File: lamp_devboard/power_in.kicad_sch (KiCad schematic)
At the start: 26 parts, among them J201 Screw_Terminal_01x02, J202 USB_C_Receptacle_USB2.0, U201 TLV71318PDBV, U202 TLV71318PDBV, U203 FUSB302B01MPX

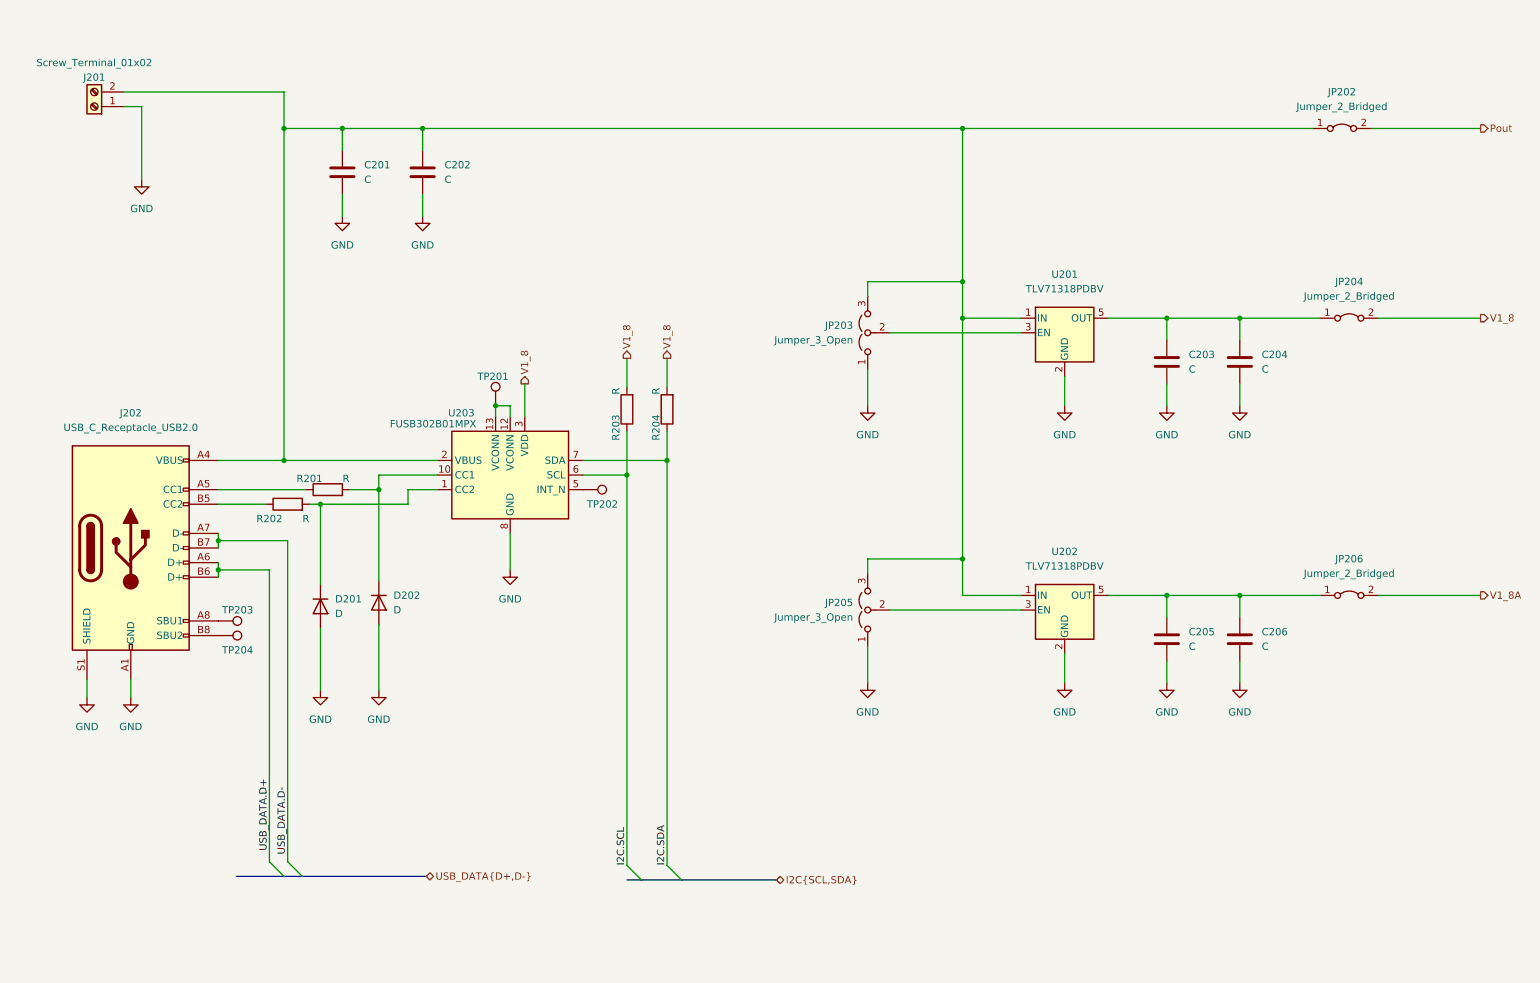
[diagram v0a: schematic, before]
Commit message: schematics, add battery to power module
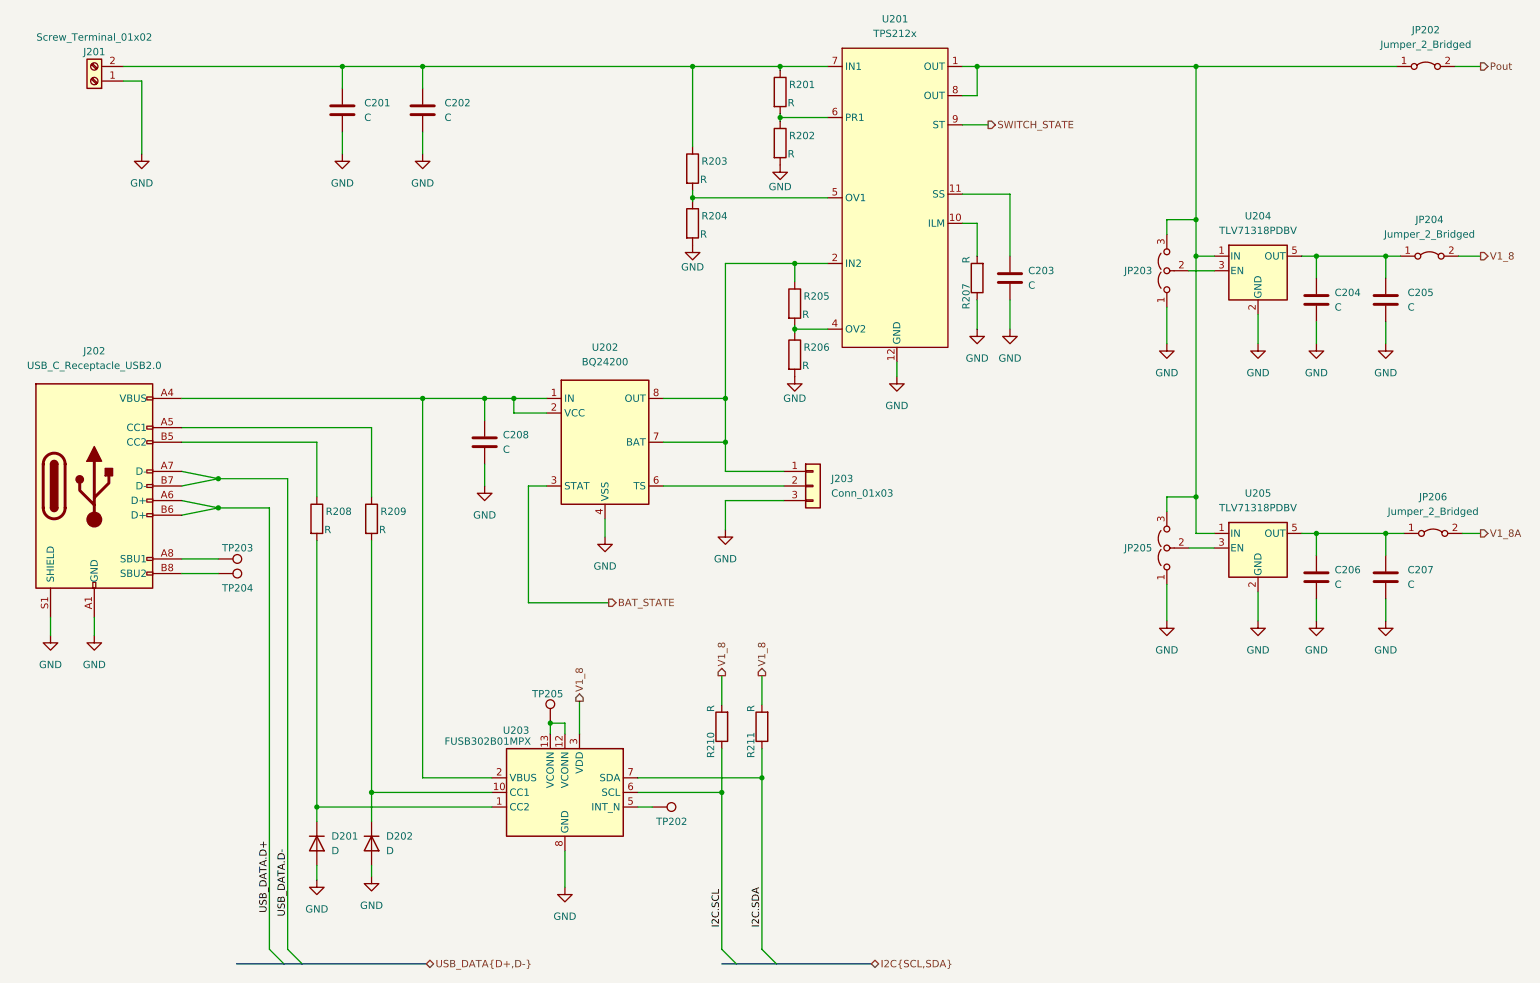
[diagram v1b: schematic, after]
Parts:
- added C203: C, Capacitor_SMD:C_0603_1608Metric_Pad1.08x0.95mm_HandSolder, symbol Device:C
- added C208: C, Capacitor_SMD:C_2220_5650Metric_Pad1.97x5.40mm_HandSolder, symbol Device:C
- added J203: Conn_01x03, Connector_Molex:Molex_KK-254_AE-6410-03A_1x03_P2.54mm_Vertical, symbol Connector_Generic:Conn_01x03
- added R201, R202, R203, R204, R205, R206, R207: R, Resistor_SMD:R_0603_1608Metric_Pad0.98x0.95mm_HandSolder, symbol Device:R
- added U201: TPS212x, lamp_devboard_lib:VQFN-HR, symbol lamp_devboard_lib:TPS212x
- added U202: BQ24200, Package_SO:HVSSOP-10-1EP_3x3mm_P0.5mm_EP1.57x1.88mm_ThermalVias, symbol lamp_devboard_lib:BQ24200
- C204: renamed from C203; footprint (none) -> Capacitor_SMD:C_0603_1608Metric_Pad1.08x0.95mm_HandSolder
- C205: renamed from C204; footprint Capacitor_SMD:C_2220_5650Metric_Pad1.97x5.40mm_HandSolder -> Capacitor_SMD:C_1206_3216Metric_Pad1.33x1.80mm_HandSolder
- C207: renamed from C206; footprint Capacitor_SMD:C_2220_5650Metric_Pad1.97x5.40mm_HandSolder -> Capacitor_SMD:C_1206_3216Metric_Pad1.33x1.80mm_HandSolder
- renumbered C205 to C206, R202 to R208, R201 to R209, R203 to R210, R204 to R211, TP201 to TP205, U201 to U204, U202 to U205
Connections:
- net GND: now also C203.2, C208.2, J203.3 (Pin_3), R202.2, R204.2, R206.2, R207.1, U201.12 (GND), U202.4 (VSS)
- new net: C201.1, C202.1, J201.2 (Pin_2), R201.1, R203.1, U201.7 (IN1)
- new net: C208.1, J202.A4 (VBUS), J202.A9 (VBUS), J202.B4 (VBUS), J202.B9 (VBUS), U202.1 (IN), U202.2 (VCC), U203.2 (VBUS)
- new net: JP202.1 (A), JP203.3 (B), JP205.3 (B), U201.1 (OUT), U201.8 (OUT), U204.1 (IN), U205.1 (IN)
- new net: R201.2, R202.1, U201.6 (PR1)
- new net: R203.2, R204.1, U201.5 (OV1)
- new net: R205.2, R206.1, U201.4 (OV2)
- new net: R207.2, U201.10 (ILM)
- new net: C203.1, U201.11 (SS)
- new net: J203.1 (Pin_1), R205.1, U201.2 (IN2), U202.7 (BAT), U202.8 (OUT)
- new net: J203.2 (Pin_2), U202.6 (TS)
- new net BAT_STATE: U202.3 (STAT)
- new net SWITCH_STATE: U201.9 (ST)
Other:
- moved on the sheet: C201, C202, C204, C205, C206, C207, D201, D202, J201, J202, JP202, JP203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

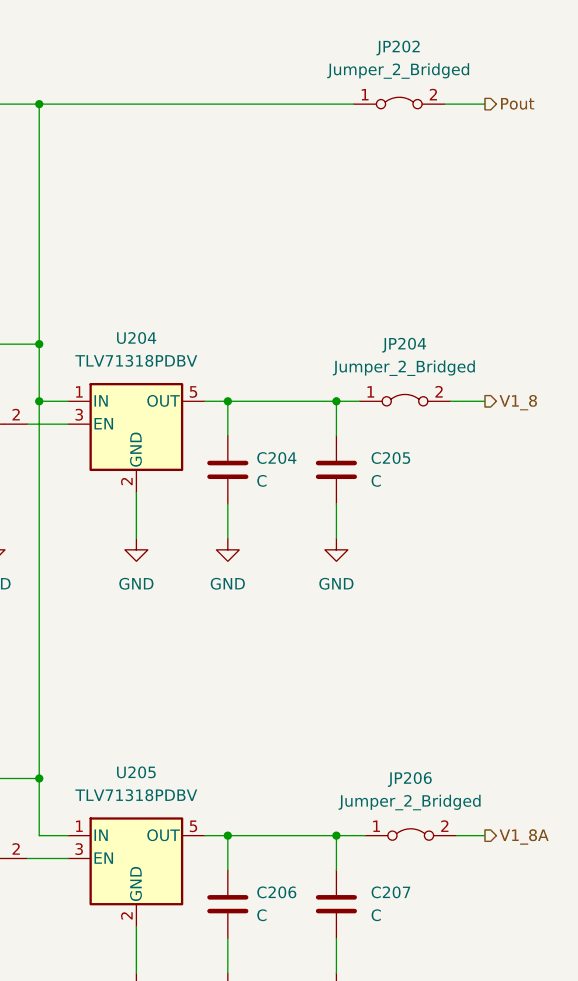
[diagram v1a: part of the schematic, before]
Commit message: place components
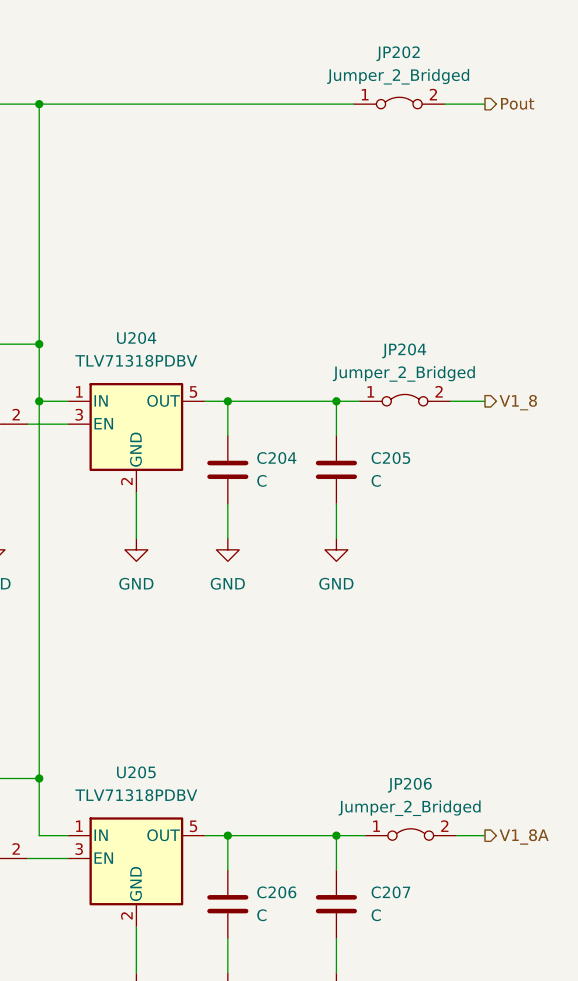
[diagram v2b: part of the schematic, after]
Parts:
- C202, C208: footprint Capacitor_SMD:C_2220_5650Metric_Pad1.97x5.40mm_HandSolder -> Capacitor_SMD:C_0603_1608Metric_Pad1.08x0.95mm_HandSolder
- JP202, JP204, JP206: footprint Connector_PinHeader_2.54mm:PinHeader_1x02_P2.54mm_Vertical -> Jumper:SolderJumper-2_P1.3mm_Bridged_RoundedPad1.0x1.5mm
- JP203, JP205: footprint Connector_PinHeader_2.54mm:PinHeader_1x03_P2.54mm_Vertical -> Jumper:SolderJumper-3_P1.3mm_Open_RoundedPad1.0x1.5mm
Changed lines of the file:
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@@
       (effects (font (size 1.27 1.27)) (justify left))
     )
-    (property "Footprint" "Capacitor_SMD:C_2220_5650Metric_Pad1.97x5.40mm_HandSolder" (id 2) (at 83.5152 38.735 0)
+    (property "Footprint" "Capacitor_SMD:C_0603_1608Metric_Pad1.08x0.95mm_HandSolder" (id 2) (at 83.5152 38.735 0)
       (effects (font (size 1.27 1.27)) hide)
     )
@@
   (symbol (lib_name "Jumper_2_Bridged_1") (lib_id "Jumper:Jumper_2_Bridged") (at 257.175 27.305 0) (unit 1)
     (in_bom yes) (on_board yes) (fields_autoplaced)
-    (property "Reference" "JP202" (id 0) (at 257.175 20.955 0))
-    (property "Value" "Jumper_2_Bridged" (id 1) (at 257.175 23.495 0))
-    (property "Footprint" "Connector_PinHeader_2.54mm:PinHeader_1x02_P2.54mm_Vertical" (id 2) (at 256.54 30.48 0)
+    (property "Reference" "JP202" (id 0) (at 257.175 21.59 0))
+    (property "Value" "Jumper_2_Bridged" (id 1) (at 257.175 24.13 0))
+    (property "Footprint" "Jumper:SolderJumper-2_P1.3mm_Bridged_RoundedPad1.0x1.5mm" (id 2) (at 256.54 30.48 0)
       (effects (font (size 1.27 1.27)) hide)
     )
@@
   (symbol (lib_name "Jumper_2_Bridged_2") (lib_id "Jumper:Jumper_2_Bridged") (at 257.81 60.325 0) (unit 1)
     (in_bom yes) (on_board yes) (fields_autoplaced)
-    (property "Reference" "JP204" (id 0) (at 257.81 53.975 0))
-    (property "Value" "Jumper_2_Bridged" (id 1) (at 257.81 56.515 0))
-    (property "Footprint" "Connector_PinHeader_2.54mm:PinHeader_1x02_P2.54mm_Vertical" (id 2) (at 257.81 63.5 0)
+    (property "Reference" "JP204" (id 0) (at 257.81 54.61 0))
+    (property "Value" "Jumper_2_Bridged" (id 1) (at 257.81 57.15 0))
+    (property "Footprint" "Jumper:SolderJumper-2_P1.3mm_Bridged_RoundedPad1.0x1.5mm" (id 2) (at 257.81 63.5 0)
       (effects (font (size 1.27 1.27)) hide)
     )
@@
       (effects (font (size 1.27 1.27)) (justify left) hide)
     )
-    (property "Footprint" "Connector_PinHeader_2.54mm:PinHeader_1x03_P2.54mm_Vertical" (id 2) (at 212.09 111.125 0)
+    (property "Footprint" "Jumper:SolderJumper-3_P1.3mm_Open_RoundedPad1.0x1.5mm" (id 2) (at 212.09 111.125 0)
       (effects (font (size 1.27 1.27)) hide)
     )
@@
   (symbol (lib_id "Jumper:Jumper_2_Bridged") (at 258.445 108.585 0) (unit 1)
     (in_bom yes) (on_board yes) (fields_autoplaced)
-    (property "Reference" "JP206" (id 0) (at 258.445 102.235 0))
-    (property "Value" "Jumper_2_Bridged" (id 1) (at 258.445 104.775 0))
-    (property "Footprint" "Connector_PinHeader_2.54mm:PinHeader_1x02_P2.54mm_Vertical" (id 2) (at 258.445 113.665 0)
+    (property "Reference" "JP206" (id 0) (at 258.445 102.87 0))
+    (property "Value" "Jumper_2_Bridged" (id 1) (at 258.445 105.41 0))
+    (property "Footprint" "Jumper:SolderJumper-2_P1.3mm_Bridged_RoundedPad1.0x1.5mm" (id 2) (at 258.445 113.665 0)
       (effects (font (size 1.27 1.27)) hide)
     )
@@
       (effects (font (size 1.27 1.27)) (justify left) hide)
     )
-    (property "Footprint" "Connector_PinHeader_2.54mm:PinHeader_1x03_P2.54mm_Vertical" (id 2) (at 212.09 62.865 0)
+    (property "Footprint" "Jumper:SolderJumper-3_P1.3mm_Open_RoundedPad1.0x1.5mm" (id 2) (at 212.09 62.865 0)
       (effects (font (size 1.27 1.27)) hide)
     )
@@
       (effects (font (size 1.27 1.27)) (justify left))
     )
-    (property "Footprint" "Capacitor_SMD:C_2220_5650Metric_Pad1.97x5.40mm_HandSolder" (id 2) (at 94.3102 96.52 0)
-      (effects (font (size 1.27 1.27)) hide)
-    )
+    (property "Footprint" "Capacitor_SMD:C_0603_1608Metric_Pad1.08x0.95mm_HandSolder" (id 2) (at 94.3102 96.52 0)
+      (effects (font (size 1.27 1.27)) hide)
+    )

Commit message: add net classes, working on pcb layout
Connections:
- net V1_8_: now reaches C204.1, C205.1, JP204.1 (A), U204.5 (OUT)
- net TerminalPIn: now reaches C201.1, C202.1, J201.2 (Pin_2), R201.1, R203.1, U201.7 (IN1)
- net UsbPIn: now reaches C208.1, J202.A4 (VBUS), J202.A9 (VBUS), J202.B4 (VBUS), J202.B9 (VBUS), U202.1 (IN), U202.2 (VCC), U203.2 (VBUS)
- net Pout_: now reaches JP202.1 (A), JP203.3 (B), JP205.3 (B), U201.1 (OUT), U201.8 (OUT), U204.1 (IN), U205.1 (IN)
- net V1_8A_: now reaches C206.1, C207.1, JP206.1 (A), U205.5 (OUT)
- net BatP: now reaches J203.1 (Pin_1), R205.1, U201.2 (IN2), U202.7 (BAT), U202.8 (OUT)
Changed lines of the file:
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@@
+    (effects (font (size 1.27 1.27)) (justify left bottom))
+  )
+  (label "Pout_" (at 196.85 27.305 0)
     (effects (font (size 1.27 1.27)) (justify left bottom))
   )
@@
     (effects (font (size 1.27 1.27)) (justify left bottom))
   )
+  (label "TerminalPIn" (at 45.72 27.305 0)
+    (effects (font (size 1.27 1.27)) (justify left bottom))
+  )
+  (label "V1_8A_" (at 241.935 108.585 0)
+    (effects (font (size 1.27 1.27)) (justify left bottom))
+  )
+  (label "V1_8_" (at 240.665 60.325 0)
+    (effects (font (size 1.27 1.27)) (justify left bottom))
+  )
+  (label "BatP" (at 127.635 85.09 0)
+    (effects (font (size 1.27 1.27)) (justify left bottom))
+  )
+  (label "UsbPIn" (at 46.355 85.09 0)
+    (effects (font (size 1.27 1.27)) (justify left bottom))
+  )

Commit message: some changes
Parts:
- removed JP203, JP205: Jumper_3_Open, Jumper:SolderJumper-3_P1.3mm_Open_RoundedPad1.0x1.5mm, symbol Jumper:Jumper_3_Open
- removed TP202, TP203, TP204, TP205: TestPoint, TestPoint:TestPoint_Pad_1.0x1.0mm, symbol Connector:TestPoint
- added D203: SM6T12A, Diode_SMD:D_SMB, symbol Diode:SM6T12A
- added F201: Fuse, Fuse:Fuse_1206_3216Metric_Pad1.42x1.75mm_HandSolder, symbol Device:Fuse
- added U207: USBLC6-4SC6, Package_TO_SOT_SMD:SOT-23-6, symbol Power_Protection:USBLC6-4SC6
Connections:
- net BatP: now also R201.1, R203.1, U201.7 (IN1); no longer R205.1, U201.2 (IN2)
- net GND: now also D203.2 (A2), U207.2 (GND)
- net Pout_: now also U204.3 (EN), U205.3 (EN)
- net TerminalPIn: now also R205.1, U201.2 (IN2), D203.1 (A1), F201.2; no longer J201.2 (Pin_2), R201.1, R203.1, U201.7 (IN1)
- net USB_DATA.D+: now also U207.6 (I/O4)
- net USB_DATA.D-: now also U207.4 (I/O3)
- net UsbPIn: now also U207.5 (VBUS)
- net at J202.A5 (CC1), R209.1: now also U207.3 (I/O2)
- net at J202.B5 (CC2), R208.1: now also U207.1 (I/O1)
- new net TerminalPIn_: F201.1, J201.2 (Pin_2)
- no-connect marks 0 -> 4
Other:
- moved on the sheet: C201, C202, C203, C204, C205, C206, C207, C208, D201, D202, J201, J202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

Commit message: some small changes
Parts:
- removed J201: Screw_Terminal_01x02, TerminalBlock:TerminalBlock_bornier-2_P5.08mm, symbol Connector:Screw_Terminal_01x02
- added J201: Conn_02x02_Counter_Clockwise, Connector_PinSocket_2.54mm:PinSocket_2x02_P2.54mm_Vertical, symbol Connector_Generic:Conn_02x02_Counter_Clockwise
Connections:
- net GND: now also J201.1 (Pin_1), J201.2 (Pin_2)
- net TerminalPIn_: now also J201.3 (Pin_3), J201.4 (Pin_4)
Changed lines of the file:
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@@
 (kicad_sch (version 20211123) (generator eeschema)
   (paper "A3")
+  (junction (at 45.085 212.09) (diameter 0) (color 0 0 0 0)
+  )
   (junction (at 336.55 78.105) (diameter 0) (color 0 0 0 0)
   )
+  (junction (at 45.085 199.39) (diameter 0) (color 0 0 0 0)
+  )
   (junction (at 336.55 111.125) (diameter 0) (color 0 0 0 0)
   )
@@
   )
   (junction (at 77.47 38.735) (diameter 0) (color 0 0 0 0)
+  )
+  (junction (at 42.545 212.09) (diameter 0) (color 0 0 0 0)
   )
   (junction (at 73.66 199.39) (diameter 0) (color 0 0 0 0)
@@
     (stroke (width 0) (type default) (color 0 0 0 0))
   )
-  (wire (pts (xy 50.8 201.93) (xy 53.975 201.93))
+  (wire (pts (xy 41.91 212.09) (xy 42.545 212.09))
     (stroke (width 0) (type default) (color 0 0 0 0))
   )
@@
     (stroke (width 0) (type default) (color 0 0 0 0))
   )
-  (wire (pts (xy 53.975 201.93) (xy 53.975 214.63))
+  (wire (pts (xy 45.085 212.09) (xy 45.085 216.535))
     (stroke (width 0) (type default) (color 0 0 0 0))
   )
@@
     (stroke (width 0) (type default) (color 0 0 0 0))
   )
+  (wire (pts (xy 42.545 212.09) (xy 45.085 212.09))
+    (stroke (width 0) (type default) (color 0 0 0 0))
+  )
   (wire (pts (xy 264.16 78.105) (xy 272.415 78.105))
     (stroke (width 0) (type default) (color 0 0 0 0))
@@
     (stroke (width 0) (type default) (color 0 0 0 0))
   )
+  (wire (pts (xy 45.085 199.39) (xy 64.135 199.39))
+    (stroke (width 0) (type default) (color 0 0 0 0))
+  )
   (bus (pts (xy 116.84 137.16) (xy 125.095 137.16))
     (stroke (width 0) (type default) (color 0 0 0 0))
@@
     (stroke (width 0) (type default) (color 0 0 0 0))
   )
-  (wire (pts (xy 64.135 199.39) (xy 50.8 199.39))
+  (wire (pts (xy 42.545 199.39) (xy 45.085 199.39))
     (stroke (width 0) (type default) (color 0 0 0 0))
   )
@@
     (pin "2")
   )
-  (symbol (lib_id "power:GND") (at 53.975 214.63 0) (unit 1)
-    (in_bom yes) (on_board yes) (fields_autoplaced)
-    (property "Reference" "#PWR0107" (id 0) (at 53.975 220.98 0)
-      (effects (font (size 1.27 1.27)) hide)
-    )
-    (property "Value" "GND" (id 1) (at 53.975 219.71 0))
-    (property "Footprint" "" (id 2) (at 53.975 214.63 0)
-      (effects (font (size 1.27 1.27)) hide)
-    )
-    (property "Datasheet" "" (id 3) (at 53.975 214.63 0)
+  (symbol (lib_id "power:GND") (at 45.085 216.535 0) (unit 1)
+    (in_bom yes) (on_board yes) (fields_autoplaced)
+    (property "Reference" "#PWR0107" (id 0) (at 45.085 222.885 0)
+      (effects (font (size 1.27 1.27)) hide)
+    )
+    (property "Value" "GND" (id 1) (at 45.085 221.615 0))
+    (property "Footprint" "" (id 2) (at 45.085 216.535 0)
+      (effects (font (size 1.27 1.27)) hide)
+    )
+    (property "Datasheet" "" (id 3) (at 45.085 216.535 0)
       (effects (font (size 1.27 1.27)) hide)
     )
@@
     )
     (pin "1")
-  )
-  (symbol (lib_id "Connector:Screw_Terminal_01x02") (at 45.72 201.93 180) (unit 1)
-    (in_bom yes) (on_board yes)
-    (property "Reference" "J201" (id 0) (at 45.72 196.85 0))
-    (property "Value" "Screw_Terminal_01x02" (id 1) (at 45.72 194.31 0))
-    (property "Footprint" "TerminalBlock:TerminalBlock_bornier-2_P5.08mm" (id 2) (at 46.355 198.12 0)
-      (effects (font (size 1.27 1.27)) hide)
-    )
-    (property "Datasheet" "~" (id 3) (at 45.72 201.93 0)
-      (effects (font (size 1.27 1.27)) hide)
-    )
-    (pin "1")
-    (pin "2")
   )
   (symbol (lib_id "Device:R") (at 266.7 119.38 0) (unit 1)
@@
     (pin "1")
   )
+  (symbol (lib_id "Connector_Generic:Conn_02x02_Counter_Clockwise") (at 42.545 207.01 90) (unit 1)
+    (in_bom yes) (on_board yes)
+    (property "Reference" "J201" (id 0) (at 36.195 205.74 90)
+      (effects (font (size 1.27 1.27)) (justify right))
+    )
+    (property "Value" "Conn_02x02_Counter_Clockwise" (id 1) (at 47.625 207.0099 90)
+      (effects (font (size 1.27 1.27)) (justify right) hide)
+    )
+    (property "Footprint" "Connector_PinSocket_2.54mm:PinSocket_2x02_P2.54mm_Vertical" (id 2) (at 42.545 207.01 0)
+      (effects (font (size 1.27 1.27)) hide)
+    )
+    (property "Datasheet" "~" (id 3) (at 42.545 207.01 0)
+      (effects (font (size 1.27 1.27)) hide)
+    )
+    (pin "1")
+    (pin "2")
+    (pin "3")
+    (pin "4")
+  )
 )
